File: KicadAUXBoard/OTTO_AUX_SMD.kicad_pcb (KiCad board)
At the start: 2 copper layers, 288.5 x 95 mm, 211 parts, among them J1 Conn_02x05_Odd_Even, J1_KD028QVFMA17 Conn_02x25_Counter_Clockwise, J2 Conn_02x05_Odd_Even, Q1 AO3400A, SW1 ALPS SKHC, SW10 ALPS SKHC, SW11 ALPS SKHC, SW12 ALPS SKHC, SW13 ALPS SKHC, SW14 ALPS SKHC, SW15 ALPS SKHC, SW16 ALPS SKHC, SW17 ALPS SKHC, SW18 ALPS SKHC, SW19 ALPS SKHC, SW2 ALPS SKHC, SW20 ALPS SKHC, SW21 ALPS SKHC, SW22 ALPS SKHC, SW23 ALPS SKHC, SW24 ALPS SKHC, SW25 ALPS SKHC, SW26 ALPS SKHC, SW27 6x6x13mm, SW28 6x6x13mm, SW29 6x6x13mm, SW3 ALPS SKHC, SW30 6x6x13mm, SW31 6x6x13mm, SW32 6x6x13mm, SW33 6x6x13mm, SW34 6x6x13mm, SW35 6x6x13mm, SW36 6x6x13mm, SW37 6x6x13mm, SW38 6x6x13mm, SW39 6x6x13mm, SW4 ALPS SKHC, SW40 6x6x13mm, SW41 6x6x13mm, SW42 6x6x13mm, SW43 6x6x13mm, SW44 6x6x13mm, SW45 6x6x13mm, SW46 6x6x13mm, SW47 6x6x13mm, SW5 ALPS SKHC, SW50 6x6x13mm, SW51 6x6x13mm, SW52 6x6x13mm, SW53 6x6x13mm, SW54 6x6x13mm, SW55 6x6x13mm, SW56 6x6x13mm, SW6 ALPS SKHC, SW7 ALPS SKHC, SW8 ALPS SKHC, SW9 ALPS SKHC, U1 SN74LV1T34_SOT-23_A, U2 TPS22918_SOT23-6_A

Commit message: LEDs Rotated
All LEDs have had their footprint and board orientation turned 180 degrees, to comply with assembly. Note that the 3rd pin has the marking on the physical part.
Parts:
- turned LED1 to 0 degrees
- turned LED10 to 0 degrees
- turned LED11 to 0 degrees
- turned LED12 to 0 degrees
- turned LED13 to 0 degrees
- turned LED14 to 0 degrees
- turned LED15 to 0 degrees
- turned LED16 to 0 degrees
- turned LED17 to 0 degrees
- turned LED18 to 0 degrees
- turned LED19 to 0 degrees
- turned LED2 to 0 degrees
- turned LED20 to 0 degrees
- turned LED21 to 0 degrees
- turned LED22 to 0 degrees
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
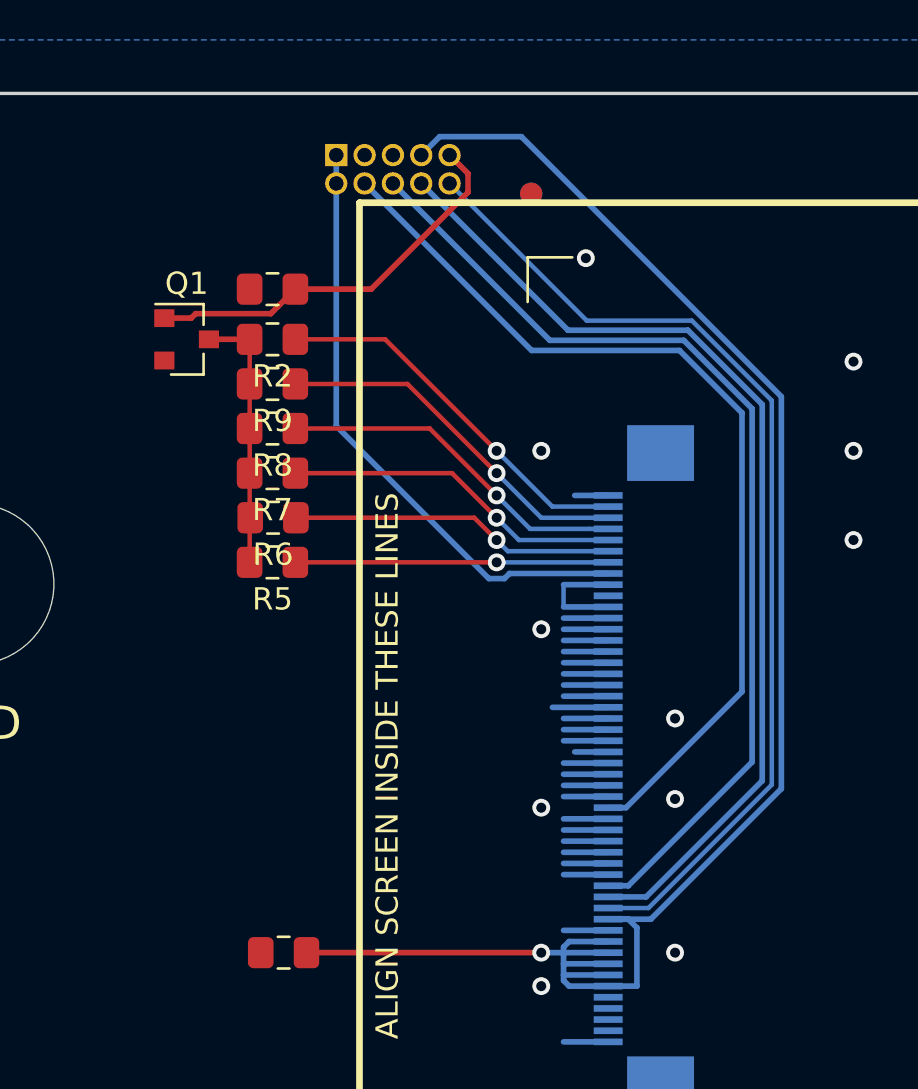
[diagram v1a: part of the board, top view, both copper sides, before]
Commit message: Moved screen header
Moved screen header to left side of screen.
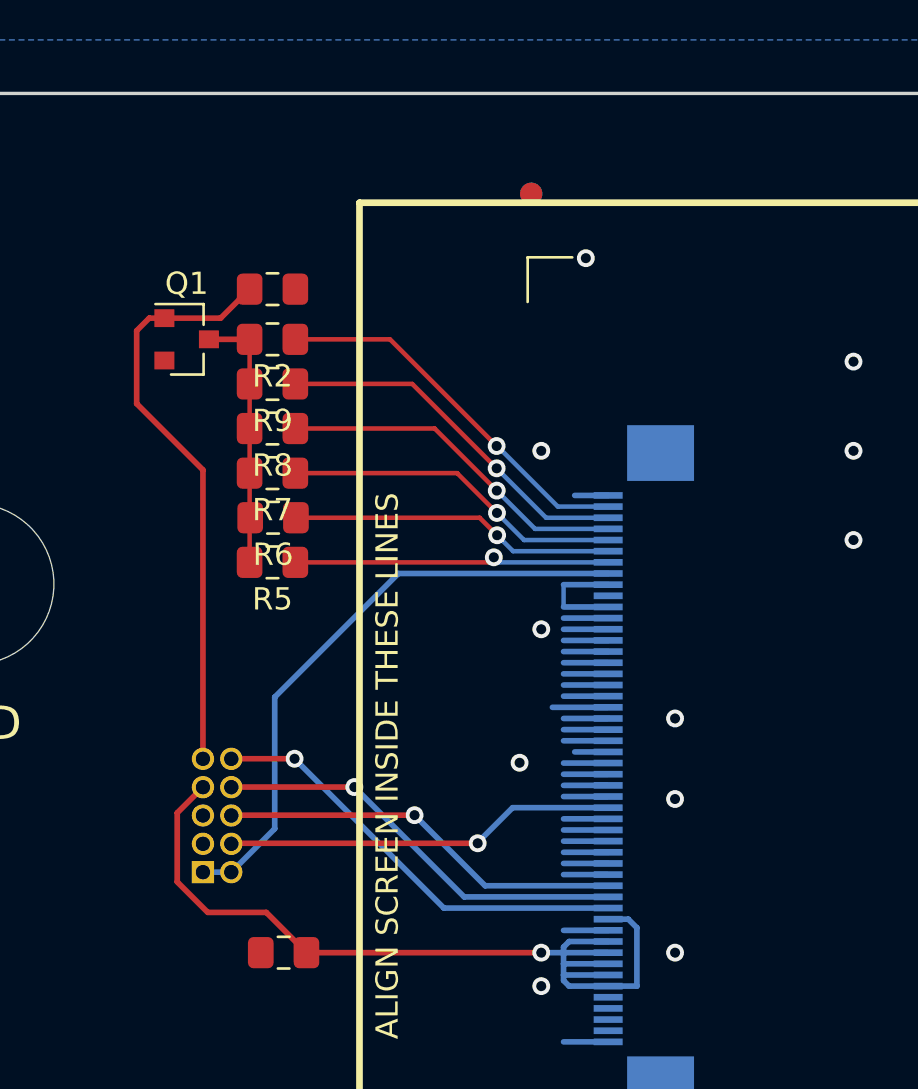
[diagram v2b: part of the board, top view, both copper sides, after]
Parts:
- J2: footprint Connector_PinHeader_1.27mm:PinHeader_2x05_P1.27mm_Vertical -> OTTO_Footprints_Lib:PinHeader_2x05_P1.27mm_Vertical
- moved J2 30.1 mm to (127.1, 42.0), turned to 0 degrees
- turned R1 to 180 degrees
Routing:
- net 3V3: track 77.7 -> 40.4 mm
- net SPI_SCLK_RASPI: track 44.9 -> 18.2 mm, vias 0 -> 1
- net SPI_CS_RASPI: track 45.3 -> 18.9 mm, vias 0 -> 1
- net RESET: track 45.3 -> 19.7 mm, vias 0 -> 1
- net SPI_MOSI_RASPI: track 41.8 -> 17.6 mm, vias 0 -> 1
- net BL_PWM: track 18.0 -> 26.3 mm

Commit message: Cutouts for mounting frontplate
Added cutouts to AUX board.
Frontplate is now the correct size under the following assumptions:
- 2mm space on left/right side of inner boards to box
- 5 mm space as above on the front side. This is mainly to allow for insertion (the power switch sticks out)
- no space on the back side
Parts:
- moved G*** 19.2 mm to (34.9, 33.7)
- moved C105 0.70 mm to (293.4, 16.8), turned to 45 degrees
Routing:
- net +5V_LEDS: track 1370.7 -> 1369.9 mm
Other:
- outline, holes or cut-outs redrawn
- board text added: "AUX BOARD V0.1.1"
- board text removed: "AUX BOARD V0.1.0"

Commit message: v0.2.0 ready for order
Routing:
- net GND: track 62.6 -> 64.6 mm
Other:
- board text added: "AUX BOARD V0.2.0"
- board text removed: "AUX BOARD V0.1.1"

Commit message: v0.3.0: various aux board fixes
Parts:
- J2: footprint OTTO_Footprints_Lib:PinHeader_2x05_P1.27mm_Vertical -> OTTO_Footprints_Lib:PinHeader_2x05_P1.27mm_Vertical_SMD
- moved H102 2.00 mm to (34.9, 99.8)
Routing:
- net 5V_BACKLIGHT: track 27.2 -> 42.1 mm
- net GND: track 64.6 -> 67.5 mm
- net 3V3: track 40.4 -> 43.1 mm, vias 1 -> 2
- net RESET: track 19.7 -> 18.4 mm, vias 1 -> 0
- net SPI_CS_RASPI: track 18.9 -> 17.6 mm, vias 1 -> 2
- net SPI_SCLK_RASPI: track 18.2 -> 16.9 mm, vias 1 -> 2
- net SPI_MOSI_RASPI: track 17.6 -> 16.3 mm, vias 1 -> 2
- net BL_PWM: track 26.3 -> 26.5 mm, vias 0 -> 1
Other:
- outline, holes or cut-outs redrawn
- board text added: "AUX BOARD V0.3.0"
- board text removed: "AUX BOARD V0.2.0"

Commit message: AUX: kbd key cutouts, screen cutout, H1-H5. Front plate: remove screw hole, mic rings footprint
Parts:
- moved G*** 0.94 mm to (34.8, 34.6)
- renumbered H5 to H4, H4 to H5
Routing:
- net +5V_LEDS: track 1369.9 -> 1372.9 mm
- net Net-(LED1-Pad2): track 15.8 -> 18.5 mm
- net Net-(LED15-Pad2): track 15.3 -> 17.3 mm
- net /LEDs/LED_CONN3: track 83.3 -> 84.2 mm

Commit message: MAIN->AUX FPC connector
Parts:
- removed J2: Conn_02x05_Odd_Even, OTTO_Footprints_Lib:PinHeader_2x05_P1.27mm_Vertical_SMD
- added FID1: Fiducial, Fiducial:Fiducial_1mm_Mask2mm, F.Cu at (47.3, -40.4)
- added FID7: Fiducial, Fiducial:Fiducial_1mm_Mask2mm, F.Cu at (50.9, -40.4)
- J1: value Conn_02x05_Odd_Even -> Conn_01x12; footprint Connector_PinHeader_1.27mm:PinHeader_2x05_P1.27mm_Vertical -> OTTO_Footprints_Lib:X10B25L12T_FPC_1x12-1MP_P1.00mm_Horizontal
- moved J1 174.4 mm to (195.3, 58.2), turned to 0 degrees
- renumbered H5 to H4, H4 to H5
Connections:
- J1 pad 1: +5V_REG -> 5V_BACKLIGHT
- J1 pad 10: GND -> /SPI_MOSI_MCU
- J1 pad 2: +5V_REG -> 3V3
- J1 pad 3: /SPI_MOSI_MCU -> SPI_MOSI_RASPI
- J1 pad 4: LED_PWR_EN -> SPI_SCLK_RASPI
- J1 pad 5: (no net) -> SPI_CS_RASPI
- J1 pad 6: (no net) -> GND
- J1 pad 7: (no net) -> RESET
- J1 pad 8: (no net) -> BL_PWM
- J1 pad 9: GND -> +5V_REG
- J1_KD028QVFMA17 pad 2: (no net) -> Net-(J1_KD028QVFMA17-Pad2)
- J1_KD028QVFMA17 pad 3: (no net) -> Net-(J1_KD028QVFMA17-Pad3)
- J1_KD028QVFMA17 pad 4: (no net) -> Net-(J1_KD028QVFMA17-Pad4)
- J1_KD028QVFMA17 pad 41: (no net) -> Net-(J1_KD028QVFMA17-Pad41)
- J1_KD028QVFMA17 pad 5: (no net) -> Net-(J1_KD028QVFMA17-Pad5)
- LED54 pad 2: (no net) -> /LEDs/LED_OUT
- U1 pad 1: (no net) -> Net-(U1-Pad1)
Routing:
- net LED_PWR_EN: track 15.8 -> 187.7 mm
- net /SPI_MOSI_MCU: track 18.9 -> 187.0 mm, vias 0 -> 1
- net +5V_REG: track 16.6 -> 174.2 mm, vias 0 -> 2
- net BL_PWM: track 26.5 -> 94.7 mm
- net RESET: track 18.4 -> 78.5 mm, vias 0 -> 2
- net SPI_CS_RASPI: track 17.6 -> 74.9 mm
- net SPI_SCLK_RASPI: track 16.9 -> 71.8 mm
- net SPI_MOSI_RASPI: track 16.3 -> 70.0 mm, vias 2 -> 0
- net 3V3: track 43.1 -> 78.8 mm, vias 2 -> 1
- net 5V_BACKLIGHT: track 42.1 -> 60.9 mm
- net GND: track 67.5 -> 64.6 mm
